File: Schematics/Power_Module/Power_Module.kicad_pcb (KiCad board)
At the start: 4 copper layers, 69.5 x 60 mm, 77 parts, among them J2 ScrewSwitch A, J3 Battery A, J4 USB_C_Female_USB2_Small, J6 Stack Male Edge Connector, J8 SWD_B, Q1 AO4447A, U1 LMR51430XDDCR, U10 ISO1042BDWVR, U12 LM66100DCKR, U14 LM66100DCKR, U15 LM66100DCKR, U2 LMR51430XDDCR, U4 STM32F103C8T6, U6 ACS37041KLHBLT-010B3, U7 ACS37041KLHBLT-010B3, U9 AMS1117-3.3

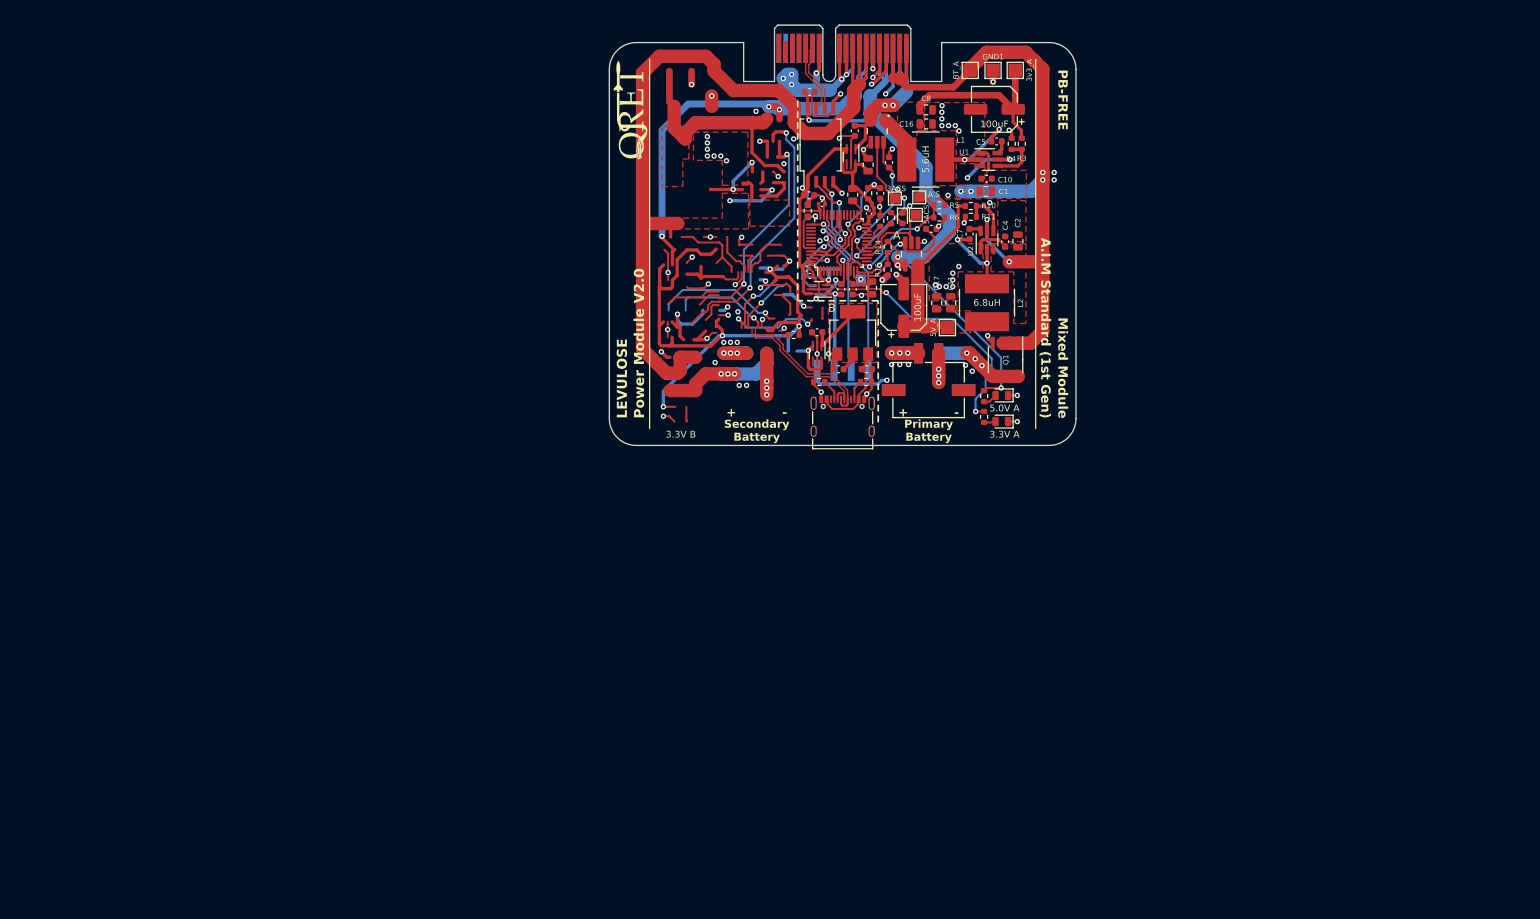
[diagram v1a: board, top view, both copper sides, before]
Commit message: started layout design  - added shunt based 24V current sensing
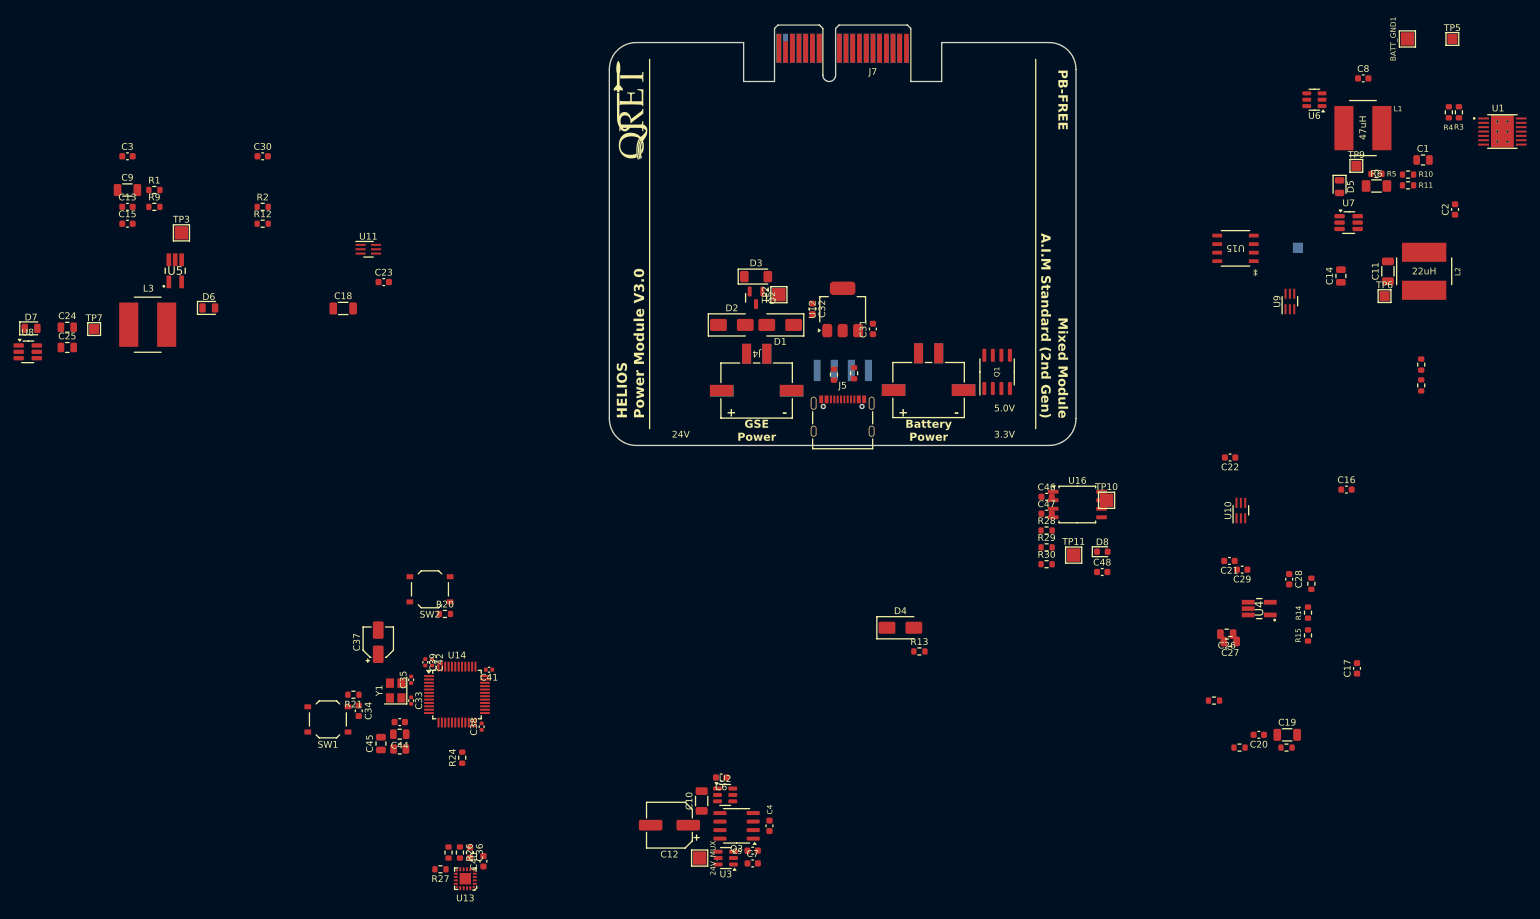
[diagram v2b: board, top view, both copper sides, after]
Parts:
- removed J8: SWD_B, SWD_Header:SWD_PinHeader_1x04_P2.54mm_Horizontal_SMD
- removed TP12: 3ACS, TestPoint:TestPoint_Pad_1.5x1.5mm
- removed TP13: 5ACS, TestPoint:TestPoint_Pad_1.5x1.5mm
- added C13: 100nF, Capacitor_SMD:C_0603_1608Metric, F.Cu at (58.5, 64.2)
- added C15: 100nF, Capacitor_SMD:C_0603_1608Metric, F.Cu at (58.5, 66.7)
- added C18: 10uF, Capacitor_SMD:C_1206_3216Metric, F.Cu at (90.6, 79.3)
- added C23: 100nF, Capacitor_SMD:C_0603_1608Metric, F.Cu at (96.7, 75.4)
- added C24: 10uF, Capacitor_SMD:C_0805_2012Metric, F.Cu at (49.5, 82.2)
- added C25: 10uF, Capacitor_SMD:C_0805_2012Metric, F.Cu at (49.5, 85.2)
- added C3: 10nF, Capacitor_SMD:C_0603_1608Metric, F.Cu at (58.5, 56.7)
- added C30: 1uF, Capacitor_SMD:C_0603_1608Metric, F.Cu at (78.6, 56.7)
- added C31: 10uF, Capacitor_SMD:C_0603_1608Metric, F.Cu at (169.5, 82.4)
- added C32: 10uF, Capacitor_SMD:C_0603_1608Metric, F.Cu at (160.5, 79.4)
- added C36: 1uF, Capacitor_SMD:C_0603_1608Metric, F.Cu at (109.5, 160.4)
- added C37: 10uF, Capacitor_SMD:CP_Elec_4x5.4, F.Cu at (95.8, 129.1)
- added C38: 100n, Capacitor_SMD:C_0402_1005Metric, F.Cu at (111.2, 141.6)
- added C39: 100n, Capacitor_SMD:C_0402_1005Metric, F.Cu at (102.8, 132.1)
- added C41: 100n, Capacitor_SMD:C_0402_1005Metric, F.Cu at (112.3, 133.2)
- added C46: 100nF, Capacitor_SMD:C_0603_1608Metric, F.Cu at (195.4, 107.4)
- added C47: 100nF, Capacitor_SMD:C_0603_1608Metric, F.Cu at (195.4, 109.9)
- added C6: 1uF, Capacitor_SMD:C_0603_1608Metric, F.Cu at (146.9, 149.2)
- added C9: 10uF, Capacitor_SMD:C_1206_3216Metric, F.Cu at (58.5, 61.7)
- added D3: BZV55C12, Diode_SMD:D_MiniMELF, F.Cu at (152.1, 74.6)
- added D4: 50V 3A, Diode_SMD:D_SMA, F.Cu at (173.6, 126.9)
- added D6: 5V PWR (RED), LED_SMD:LED_0805_2012Metric, F.Cu at (70.6, 79.3)
- added D7: 24V PWR (YLW), LED_SMD:LED_0805_2012Metric, F.Cu at (44.1, 82.3)
- added D8: DB_LED (YLW), LED_SMD:LED_0603_1608Metric, F.Cu at (203.7, 115.6)
- added J1: ScrewSwitch, footprints:CONN_2-1445057-2_TYCO, B.Cu at (176.3, 86.0)
- added J5: USB_C_Female_USB2_Small, footprints:USB_C_DB-108PWB, F.Cu at (165.0, 95.4)
- added J7: Stack Male Edge Connector, Connector_PCBEdge:BUS_PCIexpress_x1, F.Cu at (174.5, 40.6)
- added L3: 68uH, Inductor_SMD:L_Bourns_SRN8040TA, F.Cu at (61.5, 81.8)
- added Q2: TSM2309CX, Package_TO_SOT_SMD:SOT-23, F.Cu at (152.1, 77.8)
- added Q3: DMN6040SSD-13, Package_SO:SOIC-8_3.9x4.9mm_P1.27mm, F.Cu at (149.2, 156.4)
- added R1: 6.2k, Resistor_SMD:R_0603_1608Metric, F.Cu at (62.5, 61.7)
- added R12: 1k, Resistor_SMD:R_0603_1608Metric, F.Cu at (78.6, 66.7)
- added R13: 10k, Resistor_SMD:R_0603_1608Metric, F.Cu at (176.4, 130.4)
- added R2: 82k, Resistor_SMD:R_0603_1608Metric, F.Cu at (78.6, 64.2)
- added R20: 100k, Resistor_SMD:R_0603_1608Metric, F.Cu at (105.8, 124.8)
- added R21: 100k, Resistor_SMD:R_0603_1608Metric, F.Cu at (92.1, 136.9)
- added R26: 47k, Resistor_SMD:R_0603_1608Metric, F.Cu at (108.0, 160.4)
- added R27: 1k, Resistor_SMD:R_0603_1608Metric, F.Cu at (105.1, 162.9)
- added R28: 680R, Resistor_SMD:R_0603_1608Metric, F.Cu at (195.4, 112.4)
- added R29: 10k, Resistor_SMD:R_0603_1608Metric, F.Cu at (195.4, 114.9)
- added R30: 10k, Resistor_SMD:R_0603_1608Metric, F.Cu at (195.4, 117.4)
- added R9: 2.4k, Resistor_SMD:R_0603_1608Metric, F.Cu at (62.5, 64.2)
- added SW1: SW_STM_RESET, Button_Switch_SMD:SW_Push_1P1T_XKB_TS-1187A, F.Cu at (88.3, 140.6)
- added SW2: SW_STM_BOOT_MODE, Button_Switch_SMD:SW_Push_1P1T_XKB_TS-1187A, F.Cu at (103.5, 121.2)
- added TP10: 3v3, TestPoint:TestPoint_Pad_2.0x2.0mm, F.Cu at (204.3, 107.9)
- added TP11: 5V, TestPoint:TestPoint_Pad_2.0x2.0mm, F.Cu at (199.4, 116.1)
- added TP2: GSE_GND1, TestPoint:TestPoint_Pad_2.0x2.0mm, F.Cu at (155.5, 77.3)
- added TP3: 24V_PSU, TestPoint:TestPoint_Pad_2.0x2.0mm, F.Cu at (66.5, 68.1)
- added TP7: 3ACS, TestPoint:TestPoint_Pad_1.5x1.5mm, F.Cu at (53.5, 82.4)
- added U11: LM66100DCKR, LMR66100:SC-70-6_Handsoldering, F.Cu at (94.4, 70.5)
- added U13: CP2102N-A02-GQFN20R, digikey-footprints:QFN-20-1EP_3x3mm, F.Cu at (108.8, 164.3)
- added U16: W25Q128JVS, Package_SO:SOIC-8_5.23x5.23mm_P1.27mm, F.Cu at (199.9, 108.5)
- added U3: LM74700QDBVRQ1, Package_TO_SOT_SMD:SOT-23-6, F.Cu at (147.6, 161.2)
- added U5: ACS37041KLHBLT-010B5, footprints:APS12628LLHALTBAP_HandSolder, F.Cu at (65.6, 73.7)
- added U8: LMR51430XDDCR, Package_TO_SOT_SMD:SOT-23-6_Handsoldering, F.Cu at (43.6, 85.8)
- added Y1: X322516MMB4SI, Crystal:Crystal_SMD_3225-4Pin_3.2x2.5mm, F.Cu at (98.4, 136.2)
- C10: value 100nF -> 10uF; footprint Capacitor_SMD:C_0603_1608Metric -> Capacitor_SMD:C_1206_3216Metric
- C11: value 22uF -> 10uF; footprint Capacitor_SMD:C_0805_2012Metric -> Capacitor_SMD:C_1206_3216Metric
- C14: value 100uF -> 4.7uF; footprint Capacitor_SMD:CP_Elec_6.3x5.9 -> Capacitor_SMD:C_0805_2012Metric
- C16, C17: value 22uF -> 100nF; footprint Capacitor_SMD:C_0805_2012Metric -> Capacitor_SMD:C_0603_1608Metric
- C19: footprint Capacitor_SMD:C_0603_1608Metric -> Capacitor_SMD:C_1206_3216Metric
- C2: value 4.7uF -> 100nF; footprint Capacitor_SMD:C_0805_2012Metric -> Capacitor_SMD:C_0603_1608Metric
- C20: value 10uF -> 100nF
- C21, C22: value 0.1u -> 100nF
- C26, C27: value 100n -> 10uF; footprint Capacitor_SMD:C_0402_1005Metric -> Capacitor_SMD:C_0805_2012Metric
- C28, C29: value 100n -> 1uF; footprint Capacitor_SMD:C_0402_1005Metric -> Capacitor_SMD:C_0603_1608Metric
- C33: value 10n -> 10p; footprint Capacitor_SMD:C_0603_1608Metric -> Capacitor_SMD:C_0402_1005Metric
- C34: value 1uF -> 100nF; footprint Capacitor_SMD:C_0805_2012Metric -> Capacitor_SMD:C_0603_1608Metric
- C35: value 1uF -> 10p; footprint Capacitor_SMD:C_0805_2012Metric -> Capacitor_SMD:C_0402_1005Metric
- C4, C5, C7: value 100nF -> 1uF
- C40: value 1uF -> 10uF
- C42: value 1uF -> 100n; footprint Capacitor_SMD:C_0603_1608Metric -> Capacitor_SMD:C_0402_1005Metric
- C43: value 1uF -> 10nF
- C44, C45: value 0.1u -> 1uF; footprint Capacitor_SMD:C_0603_1608Metric -> Capacitor_SMD:C_0805_2012Metric
- C8: value 22uF -> 33nF; footprint Capacitor_SMD:C_0805_2012Metric -> Capacitor_SMD:C_0603_1608Metric
- D1: value 3.3V_A PWR (GRN) -> SMAJ30A; footprint LED_SMD:LED_0805_2012Metric -> Diode_SMD:D_SMA
- D2: value 5.0V_A PWR (RED) -> SMAJ30A; footprint LED_SMD:LED_0805_2012Metric -> Diode_SMD:D_SMA
- D5: value DB_LED (YLW) -> 3.3V PWR (GRN); footprint LED_SMD:LED_0603_1608Metric -> LED_SMD:LED_0805_2012Metric
- J2: value ScrewSwitch A -> Battery; moved to F.Cu
- J3: value Battery A -> ScrewSwitch; moved to B.Cu
- J4: value USB_C_Female_USB2_Small -> GSE; footprint footprints:USB_C_DB-108PWB -> footprints:CONN_2-1445057-2_TYCO
- J6: value Stack Male Edge Connector -> SWD_B; footprint Connector_PCBEdge:BUS_PCIexpress_x1 -> SWD_Header:SWD_PinHeader_1x04_P2.54mm_Horizontal_SMD; moved to B.Cu
- L1: value 5.6uH -> 47uH
- L2: value 6.8uH -> 22uH
- R10: value 56k -> 12K
- R11: value 7.5k -> 30k
- R14: value 30k -> 10k
- R15: value 30k -> 100k
- R16: value 5.1k -> 100k
- R17: value 5.1k -> 22k
- R18: value 1.5k -> 56k
- R19: value 680R -> 7.5k
- R22: value 10k -> 5.1k
- R23: value 100k -> 5.1k
- R24: value BT0_A -> 100k; footprint Resistor_SMD:R_0603_1608Metric_Pad0.98x0.95mm_HandSolder -> Resistor_SMD:R_0603_1608Metric; moved to F.Cu
- R25: value 100k -> 22k
- R3: value 100k -> 12k
- R4: value 22k -> 220k
- R6: value 10k -> 0.1; footprint Resistor_SMD:R_0603_1608Metric -> Resistor_SMD:R_1206_3216Metric_Pad1.30x1.75mm_HandSolder
- R7: value 3.3k -> 30k
- R8: value 2.4k -> 3.3k
- TP1: value BT_A -> BATT_GND1
- TP4: value GND1 -> 24V_MUX
- TP5: value 3v3_A -> 5VSENS; footprint TestPoint:TestPoint_Pad_2.0x2.0mm -> TestPoint:TestPoint_Pad_1.5x1.5mm
- TP6: value 5V_A -> A.S; footprint TestPoint:TestPoint_Pad_2.0x2.0mm -> TestPoint:TestPoint_Pad_1.5x1.5mm
- TP8: value 5VSENS -> 5ACS
- TP9: value A.S -> 24VSENS
- U1: value LMR51430XDDCR -> TPS61175PWPR; footprint Package_TO_SOT_SMD:SOT-23-6_Handsoldering -> footprints:IC_TPS27S100BPWPR
- U10: value ISO1042BDWVR -> LM66100DCKR; footprint ISO1042:SOIC-8 ISO1042BDWV -> LMR66100:SC-70-6_Handsoldering
- U12: value LM66100DCKR -> AMS1117-3.3; footprint LMR66100:SC-70-6_Handsoldering -> Package_TO_SOT_SMD:SOT-223-3_TabPin2
- U14: value LM66100DCKR -> STM32F103CBT6; footprint LMR66100:SC-70-6_Handsoldering -> Package_QFP:LQFP-48_7x7mm_P0.5mm
- U15: value LM66100DCKR -> ISO1044BDR; footprint LMR66100:SC-70-6_Handsoldering -> ISO1044:SOIC_1044BDR_TEX
- U2: value LMR51430XDDCR -> LM74700QDBVRQ1; footprint Package_TO_SOT_SMD:SOT-23-6_Handsoldering -> Package_TO_SOT_SMD:SOT-23-6
- U4: value STM32F103C8T6 -> ACS37041KLHBLT-010B3; footprint Package_QFP:LQFP-48_7x7mm_P0.5mm -> footprints:APS12628LLHALTBAP_HandSolder
- U6: value ACS37041KLHBLT-010B3 -> INA181A2; footprint footprints:APS12628LLHALTBAP_HandSolder -> Package_TO_SOT_SMD:SOT-23-6
- U7: value ACS37041KLHBLT-010B3 -> LMR51430XDDCR; footprint footprints:APS12628LLHALTBAP_HandSolder -> Package_TO_SOT_SMD:SOT-23-6_Handsoldering
- U9: value AMS1117-3.3 -> LM66100DCKR; footprint Package_TO_SOT_SMD:SOT-223-3_TabPin2 -> LMR66100:SC-70-6_Handsoldering
- moved TP4 125.2 mm to (143.7, 161.2), turned to -90 degrees
- moved C12 117.1 mm to (139.2, 156.3)
- moved R25 113.9 mm to (106.3, 160.4), turned to 90 degrees
- moved C45 112.2 mm to (96.2, 144.2), turned to 90 degrees
- moved C44 112.1 mm to (99.0, 142.8), turned to 180 degrees
- moved C5 111.7 mm to (151.6, 160.1)
- moved FB1 106.6 mm to (99.0, 145.0), turned to 180 degrees
- moved C35 102.5 mm to (100.7, 134.7)
- moved C10 101.9 mm to (144.0, 152.7), turned to 90 degrees
- moved C42 101.1 mm to (103.8, 132.1)
- moved U14 99.3 mm to (107.6, 136.8), turned to 0 degrees
- moved C7 99.1 mm to (151.6, 162.0), turned to 0 degrees
- moved C34 99.0 mm to (92.9, 139.3)
- moved R24 96.3 mm to (108.3, 146.2), turned to 90 degrees
- moved C4 93.8 mm to (154.1, 156.4)
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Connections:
- C1 pad 1: BATT_A -> V_BATT
- C10 pad 1: BATT_A -> 24V_MUX_Pre
- C11 pad 1: 5.0V_A_Pre -> 24V_PSU
- C12 pad 1: 3.3V_A_Pre -> 24V_MUX_Pre
- C14 pad 1: 5.0V_A_Pre -> 3.3V_MUX
- C16 pad 1: 3.3V_A_Pre -> 5V_ACS_PWR
- C17 pad 1: 5.0V_A_Pre -> 24V_CURR_SENSE
- C19 pad 1: Net-(U9-VI) -> 24V_MUX
- C2 pad 1: BATT_A -> V_BATT
- C20 pad 1: V_REGUSB_A -> 24V_MUX
- C21 pad 1: GND -> 24V_MUX
- C21 pad 2: 3.3V_MUX_A -> GND
- C22 pad 1: GND -> Net-(U7-CB)
- C22 pad 2: 5.0V_A -> Net-(U7-SW)
- C26 pad 1: GND -> 3.3V_PSU_Pre
- C26 pad 2: V_MUX_A -> GND
- C27 pad 1: GND -> 5V_PSU_Pre
- C27 pad 2: V_MUX_A -> GND
- C28 pad 1: GND -> 3.3V_PSU
- C28 pad 2: V_MUX_A -> GND
- C29 pad 1: GND -> 3.3V_SWD
- C29 pad 2: V_MUX_A -> GND
- C33 pad 1: 3.3VA_A -> OSC_IN
- C34 pad 1: 3.3VA_A -> STM_RESET
- C35 pad 1: V_MUX_A -> OSC_OUT
- C4 pad 1: BATT_A -> GND
- C4 pad 2: GND -> 24V_PSU
- C40 pad 1: 3.3V_REGUSB_A -> GND
- C40 pad 2: GND2 -> +3V3
- C42 pad 1: 3.3V_A -> GND
- C42 pad 2: GND -> 3.3V_MUX
- C43 pad 1: 3.3V_SWD_A -> 3.3VA
- C44 pad 1: 3.3V_A_ACS_PWR -> 3.3VA
- C45 pad 1: 5.0V_A_ACS_PWR -> 3.3V_MUX
- C48 pad 1: STM_RESET_A -> 3.3V_MUX
- C5 pad 1: Net-(U1-SW) -> 24V_GSE
- C5 pad 2: Net-(U1-CB) -> GND
- C7 pad 1: Net-(U2-SW) -> 24V_GSE
- C7 pad 2: Net-(U2-CB) -> GND
- C8 pad 1: 3.3V_A_Pre -> Net-(C8-Pad1)
- D1 pad 1: GND -> Net-(D1-A1)
- D1 pad 2: Net-(D1-A) -> Net-(D1-A2)
- D2 pad 2: Net-(D2-A) -> Net-(D1-A2)
- FB1 pad 1: 3.3VA_A -> 3.3VA
- FB1 pad 2: V_MUX_A -> 3.3V_MUX
- J2 pad 1: Net-(J2-Pad1) -> GND
- J2 pad 2: Net-(J2-Pad2) -> Net-(J1-Pad1)
- J3 pad 1: GND -> Net-(J3-Pad1)
- J3 pad 2: Net-(J2-Pad1) -> Net-(D1-A1)
- L1 pad 1: Net-(U1-SW) -> V_BATT
- L1 pad 2: 3.3V_A_Pre -> Net-(D4-A)
- L2 pad 1: Net-(U2-SW) -> 3.3V_PSU_Pre
- L2 pad 2: 5.0V_A_Pre -> Net-(U7-SW)
- Q1 pad 1: BATT_A -> V_BATT
- Q1 pad 2: BATT_A -> V_BATT
- Q1 pad 3: BATT_A -> V_BATT
- Q1 pad 5: Net-(J2-Pad2) -> Net-(J1-Pad2)
- Q1 pad 6: Net-(J2-Pad2) -> Net-(J1-Pad2)
- Q1 pad 7: Net-(J2-Pad2) -> Net-(J1-Pad2)
- Q1 pad 8: Net-(J2-Pad2) -> Net-(J1-Pad2)
- R10 pad 1: 5.0V_A_Pre -> 24V_MUX
- R10 pad 2: Net-(U2-FB) -> Net-(D7-A)
- R11 pad 1: Net-(U2-FB) -> V_BATT
- R11 pad 2: GND -> BATT_SENSE
- R14 pad 1: 5.0V_A -> GSE_SENSE
- R14 pad 2: 5.0V_A_SENSE -> 24V_GSE
- R15 pad 1: 5.0V_A_SENSE -> GSE_SENSE
- R16 pad 1: Net-(J4-CC1) -> 3.3V_PSU_Pre
- R16 pad 2: GND2 -> Net-(U7-FB)
- R17 pad 1: Net-(J4-CC2) -> Net-(U7-FB)
- R17 pad 2: GND2 -> GND
- R18 pad 1: 3.3V_MUX_A -> 5V_PSU_Pre
- R18 pad 2: USB_D+ -> Net-(U8-FB)
- R19 pad 1: Net-(D5-A) -> Net-(U8-FB)
- R19 pad 2: DB_LED_A -> GND
- R22 pad 1: STM_RESET_A -> Net-(J5-CC1)
- R22 pad 2: V_MUX_A -> GND
- R23 pad 1: GND -> Net-(J5-CC2)
- R23 pad 2: BOOT0_A -> GND
- R24 pad 1: V_MUX_A -> GND
- R24 pad 2: BOOT0_A -> BOOT1
- R25 pad 1: GND -> Net-(U13-VBUS)
- R25 pad 2: BOOT1_A -> 5V_USB
- R3 pad 1: 3.3V_A_Pre -> Net-(U1-FB)
- R3 pad 2: Net-(U1-FB) -> GND
- R4 pad 1: Net-(U1-FB) -> 24V_PSU
- R4 pad 2: GND -> Net-(U1-FB)
- R5 pad 1: BATT_A -> 5V_PSU
- R5 pad 2: BATT_A_SENSE -> 5V_SENSE
- R6 pad 1: BATT_A_SENSE -> 24V_MUX_Pre
- R6 pad 2: GND -> 24V_MUX
- R7 pad 1: V_MUX_A -> 5V_SENSE
- R7 pad 2: Net-(D1-A) -> GND
- R8 pad 1: 5.0V_A -> 3.3V_MUX
- R8 pad 2: Net-(D2-A) -> Net-(D5-A)
- TP1 pad 1: BATT_A -> GND
- TP4 pad 1: GND -> 24V_MUX_Pre
- TP5 pad 1: 3.3V_A_Pre -> 5V_SENSE
- TP6 pad 1: 5.0V_A_Pre -> BATT_SENSE
- TP8 pad 1: 5.0V_A_SENSE -> 5V_CURR_SENSE
- TP9 pad 1: BATT_A_SENSE -> GSE_SENSE
- U1 pad 1: GND -> Net-(D4-A)
- U1 pad 2: Net-(U1-SW) -> Net-(D4-A)
- U1 pad 3: BATT_A -> V_BATT
- U1 pad 4: Net-(U1-FB) -> V_BATT
- U1 pad 5: BATT_A -> Net-(U1-SS)
- U1 pad 6: Net-(U1-CB) -> GND
- U10 pad 1: 3.3V_MUX_A -> 3.3V_SWD
- U10 pad 2: CAN_TX -> GND
- U10 pad 3: CAN_RX -> 3.3V_MUX
- U10 pad 4: GND -> unconnected-(U10-NC-Pad4)
- U10 pad 6: CAN_- -> 3.3V_MUX
- U12 pad 1: 3.3V_REGUSB_A -> GND
- U12 pad 2: GND2 -> 3.3V_REGUSB
- U12 pad 3: 3.3V_MUX_A -> 5V_USB
- U14 pad 1: 3.3V_A -> 3.3V_MUX
- U14 pad 2: GND -> unconnected-(U14-PC13-Pad2)
- U14 pad 3: 3.3V_MUX_A -> unconnected-(U14-PC14-Pad3)
- U14 pad 5: GND -> OSC_IN
- U14 pad 6: 3.3V_MUX_A -> OSC_OUT
- U15 pad 1: 3.3V_SWD_A -> +3V3
- U15 pad 2: GND -> CAN_TX
- U15 pad 3: 3.3V_MUX_A -> CAN_RX
- U15 pad 4: unconnected-(U15-NC-Pad4) -> GND
- U15 pad 5: GND -> CAN_N
- U15 pad 6: 3.3V_MUX_A -> CAN_P
- U2 pad 1: GND -> 24V_PSU
- U2 pad 2: Net-(U2-SW) -> GND
- U2 pad 3: BATT_A -> 24V_PSU
- U2 pad 4: Net-(U2-FB) -> 24V_MUX_Pre
- U2 pad 5: BATT_A -> Net-(Q3B-G2)
- U2 pad 6: Net-(U2-CB) -> 24V_PSU
- U4 pad 1: V_MUX_A -> 3.3V_PSU_Pre
- U4 pad 2: unconnected-(U4-PC13-Pad2) -> 3.3V_PSU
- U4 pad 3: unconnected-(U4-PC14-Pad3) -> GND
- U4 pad 4: unconnected-(U4-PC15-Pad4) -> 3.3V_CURR_SENSE
- U4 pad 5: unconnected-(U4-PD0-Pad5) -> 3.3V_ACS_PWR
- U6 pad 1: 3.3V_A_Pre -> Net-(R12-Pad2)
- U6 pad 2: 3.3V_A -> GND
- U6 pad 3: GND -> 24V_MUX_Pre
- U6 pad 4: 3.3V_A_CURR_SENSE -> 24V_MUX
- U6 pad 5: 3.3V_A_ACS_PWR -> GND
- U7 pad 1: 5.0V_A -> GND
- U7 pad 2: 5.0V_A_Pre -> Net-(U7-SW)
- U7 pad 3: GND -> 24V_MUX
- U7 pad 4: 5.0V_A_CURR_SENSE -> Net-(U7-FB)
- U7 pad 5: 5.0V_A_ACS_PWR -> 24V_MUX
- U9 pad 1: GND -> 3.3V_PSU
- U9 pad 2: V_REGUSB_A -> GND
- U9 pad 3: Net-(U9-VI) -> 3.3V_MUX
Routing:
- net (no net): track 274.4 -> 0.00 mm, vias 19 -> 0
- net Net-(J6-BATT_B-PadB7): track 130.2 -> 0.00 mm, vias 2 -> 0
- net GND: track 125.9 -> 0.00 mm, vias 59 -> 0
- net BATT_A: track 125.8 -> 0.00 mm, vias 8 -> 0
- net V_MUX_A: track 106.3 -> 0.00 mm, vias 4 -> 0
- net Net-(J6-3.3V_B-PadA7): track 103.4 -> 0.00 mm, vias 3 -> 0
- net Net-(J4-CC1): track 101.1 -> 0.00 mm, vias 4 -> 0
- net 5.0V_A: track 97.4 -> 0.00 mm, vias 4 -> 0
- net GND2: track 81.2 -> 0.00 mm, vias 45 -> 0
- net Net-(J6-GND_B-PadA12): track 36.7 -> 0.00 mm, vias 6 -> 0
- net 3.3V_A_Pre: track 34.1 -> 0.00 mm
- net 3.3V_A: track 27.7 -> 0.00 mm, vias 2 -> 0
- net SWCLK_A: track 26.7 -> 0.00 mm, vias 1 -> 0
- net 5.0V_A_Pre: track 26.3 -> 0.00 mm
- net SWDIO_A: track 25.7 -> 0.00 mm, vias 1 -> 0
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- removed copper zone on F.Cu, net 3.3V_A_Pre
- removed copper zone on F.Cu, net 5.0V_A_Pre
- removed copper zone on F.Cu, net BATT_A
- removed copper zone on F.Cu, net GND
- removed copper zone on In1.Cu, net GND
- removed copper zone on In2.Cu, net GND
- removed copper zone on F.Cu, net GND2
- removed copper zone on In1.Cu, net GND2
- removed copper zone on In2.Cu, net GND2
- removed copper zone on F.Cu, net Net-(J6-3.3V_B-PadA7)
- removed copper zone on F.Cu, net Net-(J6-BATT_B-PadB7)
- removed copper zone on F.Cu, net V_REGUSB_A
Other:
- board text added: "24V"
- board text added: "3.3V"
- board text added: "5.0V"
- board text added: "A.I.M Standard (2nd Gen)"
- board text added: "Battery Power"
- board text added: "Battery Switch"
- board text added: "GSE Power"
- board text added: "GSE Switch"
- board text added: "HELIOS"
- board text added: "Power Module Rev 3.0 QRET Mar 2026 Rajan Laird Kennan Bays Oak Campbell Tristan Alderson"
- board text added: "Power Module V3.0"
- board text removed: "3.3V A"
- board text removed: "3.3V B"
- board text removed: "5.0V A"
- board text removed: "A"
- board text removed: "A.I.M Standard (1st Gen)"
- board text removed: "B"
- board text removed: "LEVULOSE"
- board text removed: "Power Module Rev 2.0 QRET Mar 2025 Rajan Laird Kennan Bays Oak Campbell"
- board text removed: "Power Module V2.0"
- board text removed: "Primary Battery"
- board text removed: "Primary Switch"
- board text removed: "Secondary Battery"
- board text removed: "Secondary Switch"

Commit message: current progress on power board
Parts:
- U10, U11, U9: footprint LMR66100:SC-70-6_Handsoldering -> LMR66100:SC-70-6
- moved U8 377.7 mm to (421.0, 69.7)
- moved C24 357.0 mm to (406.5, 83.0), turned to -90 degrees
- moved C25 355.5 mm to (404.5, 66.0), turned to 90 degrees
- moved L3 350.9 mm to (412.2, 69.7), turned to 180 degrees
- moved C18 331.2 mm to (421.8, 84.0)
- moved C23 325.4 mm to (421.9, 67.1)
- moved R16 212.6 mm to (424.8, 79.7), turned to -90 degrees
- moved R17 212.5 mm to (426.4, 79.7), turned to 90 degrees
- moved R18 208.0 mm to (425.2, 70.0), turned to -90 degrees
- moved TP11 207.7 mm to (401.4, 67.7)
- moved C20 203.3 mm to (421.0, 82.0), turned to 0 degrees
- moved C21 203.3 mm to (421.0, 72.3), turned to 0 degrees
- moved C19 202.6 mm to (421.8, 74.3)
- moved C22 200.7 mm to (421.9, 76.8)
- moved TP10 199.0 mm to (401.5, 81.5)
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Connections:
- net Net-(D1-A1) renamed /power/GSE_SW+
- net Net-(D4-A) renamed /power/BOOST_SW
- net Net-(J1-Pad1) renamed /power/BATT+
- net Net-(J1-Pad2) renamed /power/BATT_SW+
- net Net-(J3-Pad1) renamed /power/GSE+
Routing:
- net GND: track 0.00 -> 4.73 mm, vias 0 -> 18
- net Net-(U8-FB): track 0.00 -> 4.61 mm
- net Net-(D1-A2): track 0.00 -> 4.47 mm
- net Net-(U7-FB): track 0.00 -> 4.12 mm
- net /power/GSE_SW+: vias 0 -> 8
- net /power/GSE+: vias 0 -> 8
- net /power/BATT_SW+: vias 0 -> 8
- net /power/BATT+: vias 0 -> 8
- added copper zone on B.Cu, net /power/BATT+
- added copper zone on F.Cu, net /power/BATT+
- added copper zone on B.Cu, net /power/BATT_SW+
- added copper zone on F.Cu, net /power/BATT_SW+
- added copper zone on B.Cu, net /power/GSE+
- added copper zone on F.Cu, net /power/GSE+
- added copper zone on B.Cu, net /power/GSE_SW+
- added copper zone on F.Cu, net /power/GSE_SW+
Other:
- board text added: "GREG"
- board text added: "Power Module Rev 3.0 QRET Mar 2026 Rajan Laird, Kennan Bays Oak Campbell, Tristan Alderson"
- board text removed: "HELIOS"
- board text removed: "Power Module Rev 3.0 QRET Mar 2026 Rajan Laird Kennan Bays Oak Campbell Tristan Alderson"

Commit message: major layout progress, still need to place MCU
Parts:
- removed TP7: 3ACS, TestPoint:TestPoint_Pad_1.5x1.5mm
- removed TP8: 5ACS, TestPoint:TestPoint_Pad_1.5x1.5mm
- added TP12: BATT, TestPoint:TestPoint_Pad_1.5x1.5mm, F.Cu at (183.6, 43.6)
- added TP13: GSEV, TestPoint:TestPoint_Pad_1.5x1.5mm, F.Cu at (138.8, 43.6)
- R6: value 0.1 -> 100m
- TP1, TP10, TP11, TP2, TP3, TP4: footprint TestPoint:TestPoint_Pad_2.0x2.0mm -> TestPoint:TestPoint_Pad_1.5x1.5mm
- TP9: value 24VSENS -> GSE_SENS
- moved TP5 259.0 mm to (82.2, 110.4)
- moved TP9 255.4 mm to (67.7, 110.3)
- moved C18 250.6 mm to (171.8, 66.7)
- moved R16 250.6 mm to (174.8, 62.4)
- moved C20 250.6 mm to (171.0, 64.7)
- moved C24 250.6 mm to (156.5, 65.7)
- moved C26 250.6 mm to (154.2, 65.7)
- moved L2 250.6 mm to (162.2, 62.1)
- moved U7 250.6 mm to (171.0, 62.1)
- moved C22 250.6 mm to (171.9, 59.5)
- moved R17 250.6 mm to (176.4, 62.4)
- moved R14 245.6 mm to (67.5, 112.4), turned to 180 degrees
- moved R7 245.0 mm to (84.3, 111.7), turned to 90 degrees
- moved R5 244.4 mm to (82.0, 112.5)
- moved R15 243.7 mm to (69.8, 111.6), turned to 90 degrees
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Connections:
- J7 pad A15: 24V_MUX -> unconnected-(J7-Reserved-PadA15)
- J7 pad A16: 24V_MUX -> unconnected-(J7-Reserved-PadA16)
- J7 pad B15: GND -> unconnected-(J7-Reserved-PadB15)
- J7 pad B16: GND -> unconnected-(J7-Reserved-PadB16)
- J7 pad B17: GND -> unconnected-(J7-Reserved-PadB17)
- J7 pad B18: GND -> unconnected-(J7-Reserved-PadB18)
- R10 pad 1: 24V_MUX -> 24V_GSE
- U14 pad 17: DB_LED_A -> DB_LED
- U14 pad 18: unconnected-(U14-PB0-Pad18) -> GSE_SENSE
- U14 pad 19: unconnected-(U14-PB1-Pad19) -> 24V_CURR_SENSE
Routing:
- net V_BATT: track 0.00 -> 124.7 mm
- net 24V_GSE: track 0.00 -> 54.6 mm
- net GND: track 4.73 -> 36.7 mm, vias 18 -> 47
- net Net-(U1-FB): track 0.00 -> 8.23 mm
- net 24V_PSU: track 0.00 -> 5.23 mm
- net Net-(U8-FB): track 4.61 -> 0.00 mm
- net Net-(U1-SS): track 0.00 -> 4.43 mm
- net Net-(U7-FB): track 4.12 -> 0.00 mm
- net USB_D-: track 0.00 -> 3.00 mm
- net Net-(D6-A): track 0.00 -> 2.17 mm
- net Net-(U1-FREQ): track 0.00 -> 1.87 mm
- net Net-(D5-A): track 0.00 -> 1.80 mm
- net Net-(U1-COMP): track 0.00 -> 1.74 mm
- net Net-(D7-A): track 0.00 -> 1.74 mm
- net Net-(C8-Pad1): track 0.00 -> 1.50 mm
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- added copper zone on F.Cu, net /power/BOOST_SW
- added copper zone on F.Cu, net 24V_PSU
- added copper zone on F.Cu, net GND
- added copper zone on F.Cu, net V_BATT
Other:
- board text added: "C1"
- board text added: "GSEV"
- board text removed: "24V"
